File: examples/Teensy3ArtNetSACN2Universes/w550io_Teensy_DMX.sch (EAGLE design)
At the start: 33 parts, among them IC1 MAX481CPA, IC2 MAX481CPA

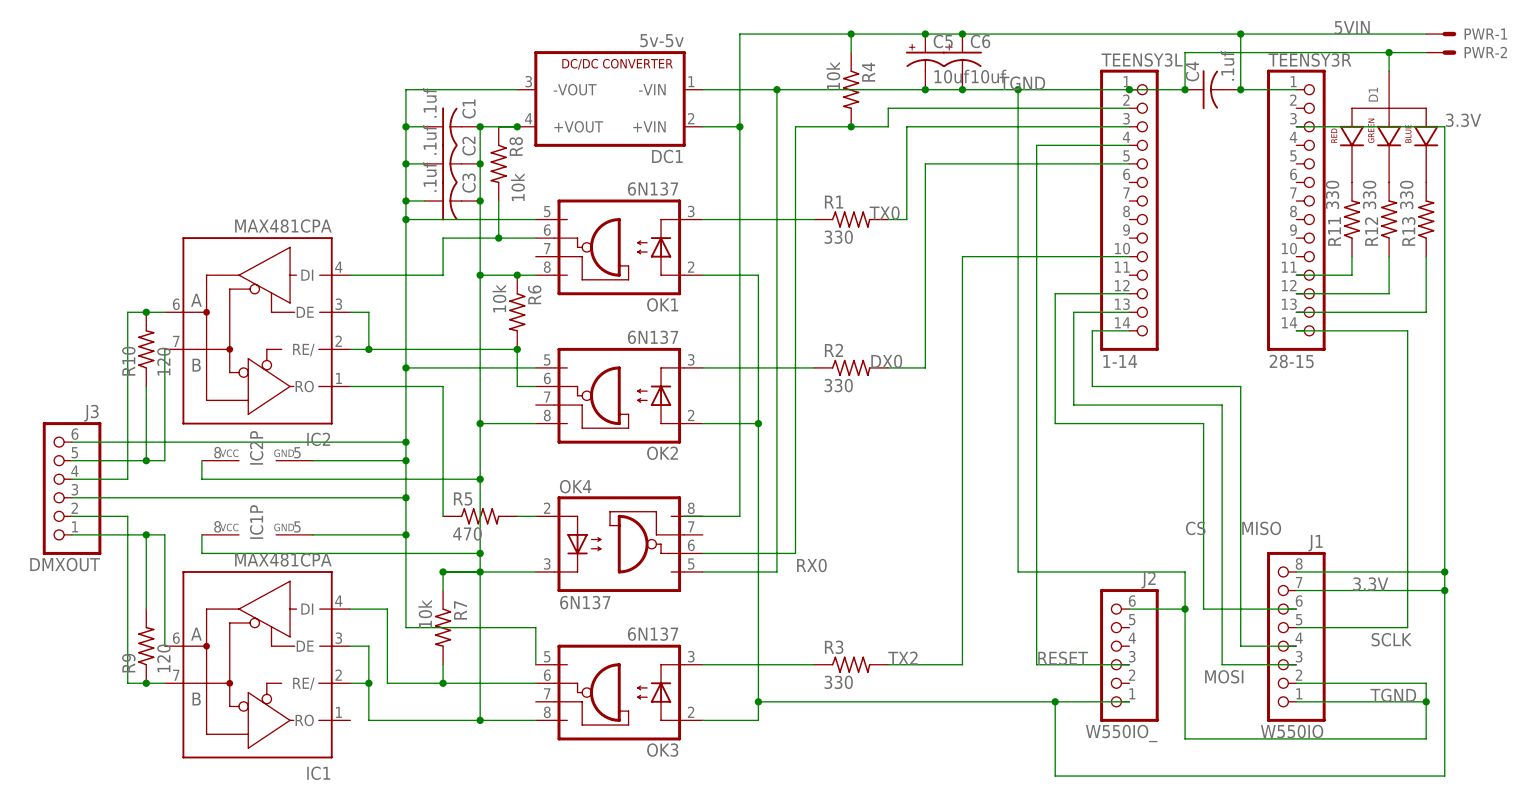
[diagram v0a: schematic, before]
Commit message: Change Board to output only
Bi-directional design power is unstable.  Previous design is functional
by not populating input and direction optocouplers.
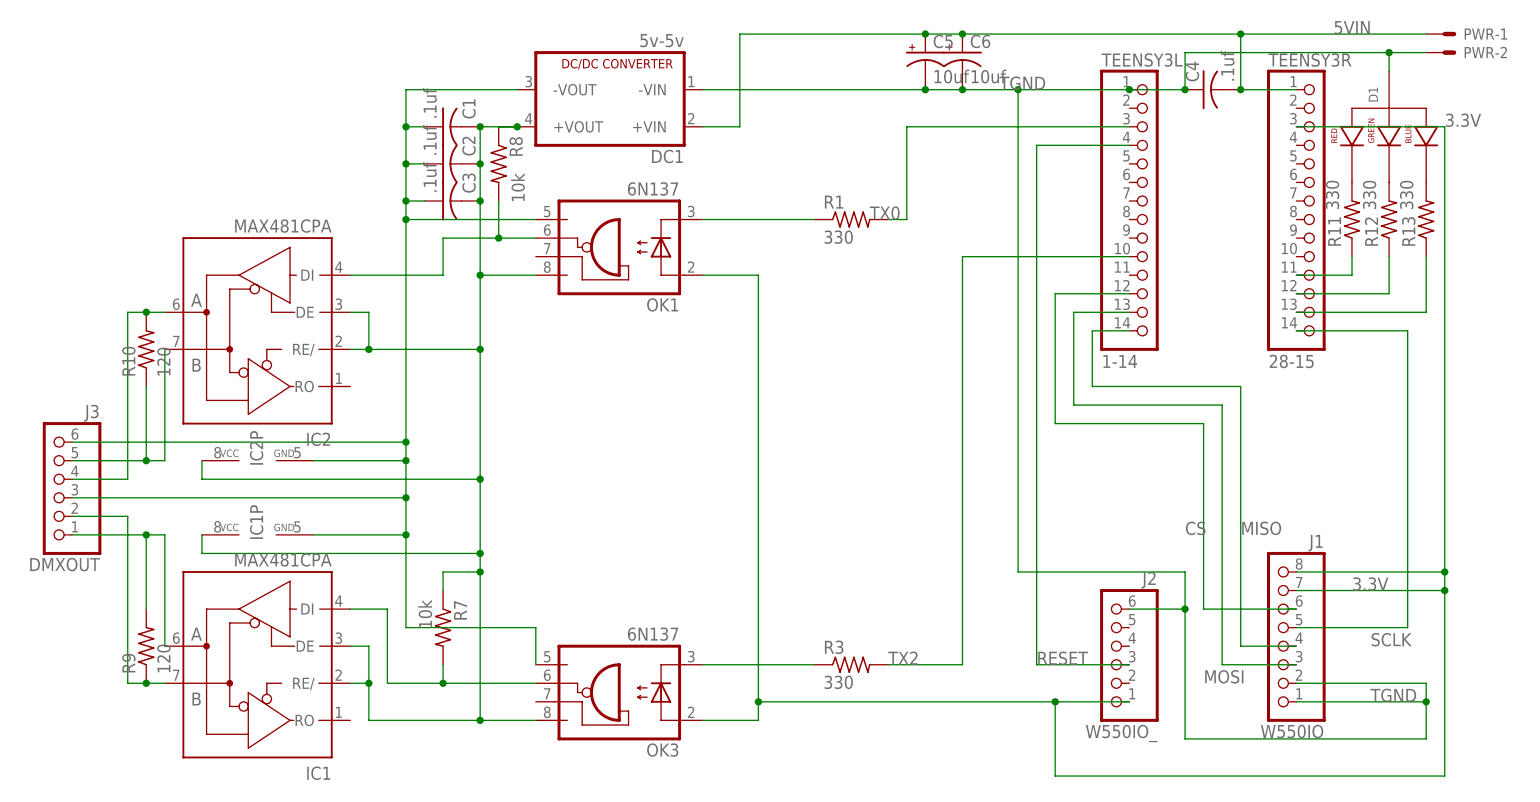
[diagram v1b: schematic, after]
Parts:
- removed OK2, OK4: 6N137, optocoupler:6N137
- removed R2: 330, adafruit:R-US_0204/5
- removed R4, R6: 10k, adafruit:R-US_0204/5
- removed R5: 470, adafruit:R-US_0204/5
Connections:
- removed net DX0: R2.2, TEENSY3L.5
- removed net N$1: OK4.A, R5.2
- removed net N$12: IC2G$1.RO, R5.1
- removed net N$13: IC2G$1.DE, IC2G$1.RE/, OK2.VO, R6.2
- removed net N$6: OK2.C, R2.1
- removed net RX0: OK4.VO, R4.2, TEENSY3L.2
- net 3.3V: no longer OK2.A
- net 5VIN: no longer R4.1
- net GND: no longer OK2.GND
- net TGND: no longer OK4.GND
- net VCC: now also IC2G$1.DE, IC2G$1.RE/; no longer OK2.VCC, OK4.C, R6.1

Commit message: Changed 10k Resistors to 1k
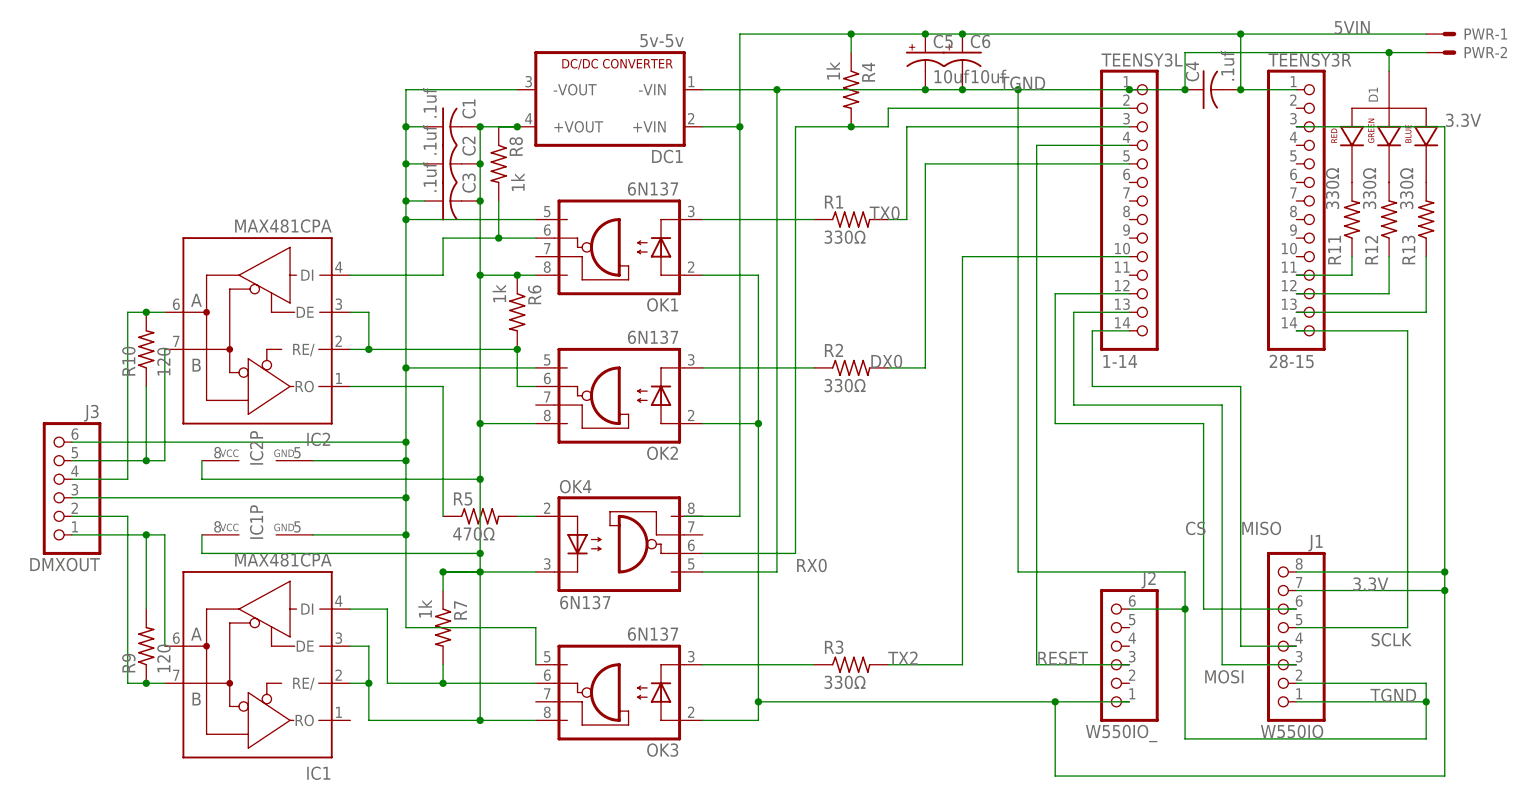
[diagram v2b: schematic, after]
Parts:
- added OK2, OK4: 6N137, optocoupler:6N137
- added R2: 330Ω, adafruit:R-US_0204/5
- added R4, R6: 1k, adafruit:R-US_0204/5
- added R5: 470Ω, adafruit:R-US_0204/5
- R1, R11, R12, R13, R3: value 330 -> 330Ω
- R7, R8: value 10k -> 1k
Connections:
- new net DX0: R2.2, TEENSY3L.5
- new net N$1: OK4.A, R5.2
- new net N$12: IC2G$1.RO, R5.1
- new net N$13: IC2G$1.DE, IC2G$1.RE/, OK2.VO, R6.2
- new net N$6: OK2.C, R2.1
- new net RX0: OK4.VO, R4.2, TEENSY3L.2
- net 3.3V: now also OK2.A
- net 5VIN: now also R4.1
- net GND: now also OK2.GND
- net TGND: now also OK4.GND
- net VCC: now also OK2.VCC, OK4.C, R6.1; no longer IC2G$1.DE, IC2G$1.RE/

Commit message: Changed resistors to 3.3k
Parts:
- R4: value 1k -> 10k
- R6, R7, R8: value 1k -> 3.3k
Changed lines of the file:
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@@
 <part name="R2" library="adafruit" deviceset="R-US_" device="0204/5" value="330Ω"/>
 <part name="R3" library="adafruit" deviceset="R-US_" device="0204/5" value="330Ω"/>
-<part name="R4" library="adafruit" deviceset="R-US_" device="0204/5" value="1k"/>
+<part name="R4" library="adafruit" deviceset="R-US_" device="0204/5" value="10k"/>
 <part name="IC1" library="maxim" deviceset="MAX481CPA" device=""/>
 <part name="IC2" library="maxim" deviceset="MAX481CPA" device=""/>
 <part name="DMXOUT" library="adafruit" deviceset="PINHD-1X6" device="B" value="J3"/>
 <part name="R5" library="adafruit" deviceset="R-US_" device="0204/5" value="470Ω"/>
-<part name="R6" library="adafruit" deviceset="R-US_" device="0204/5" value="1k"/>
-<part name="R7" library="adafruit" deviceset="R-US_" device="0204/5" value="1k"/>
-<part name="R8" library="adafruit" deviceset="R-US_" device="0204/5" value="1k"/>
+<part name="R6" library="adafruit" deviceset="R-US_" device="0204/5" value="3.3k"/>
+<part name="R7" library="adafruit" deviceset="R-US_" device="0204/5" value="3.3k"/>
+<part name="R8" library="adafruit" deviceset="R-US_" device="0204/5" value="3.3k"/>
 <part name="R9" library="adafruit" deviceset="R-US_" device="0204/5" value="120"/>
 <part name="R10" library="adafruit" deviceset="R-US_" device="0204/5" value="120"/>

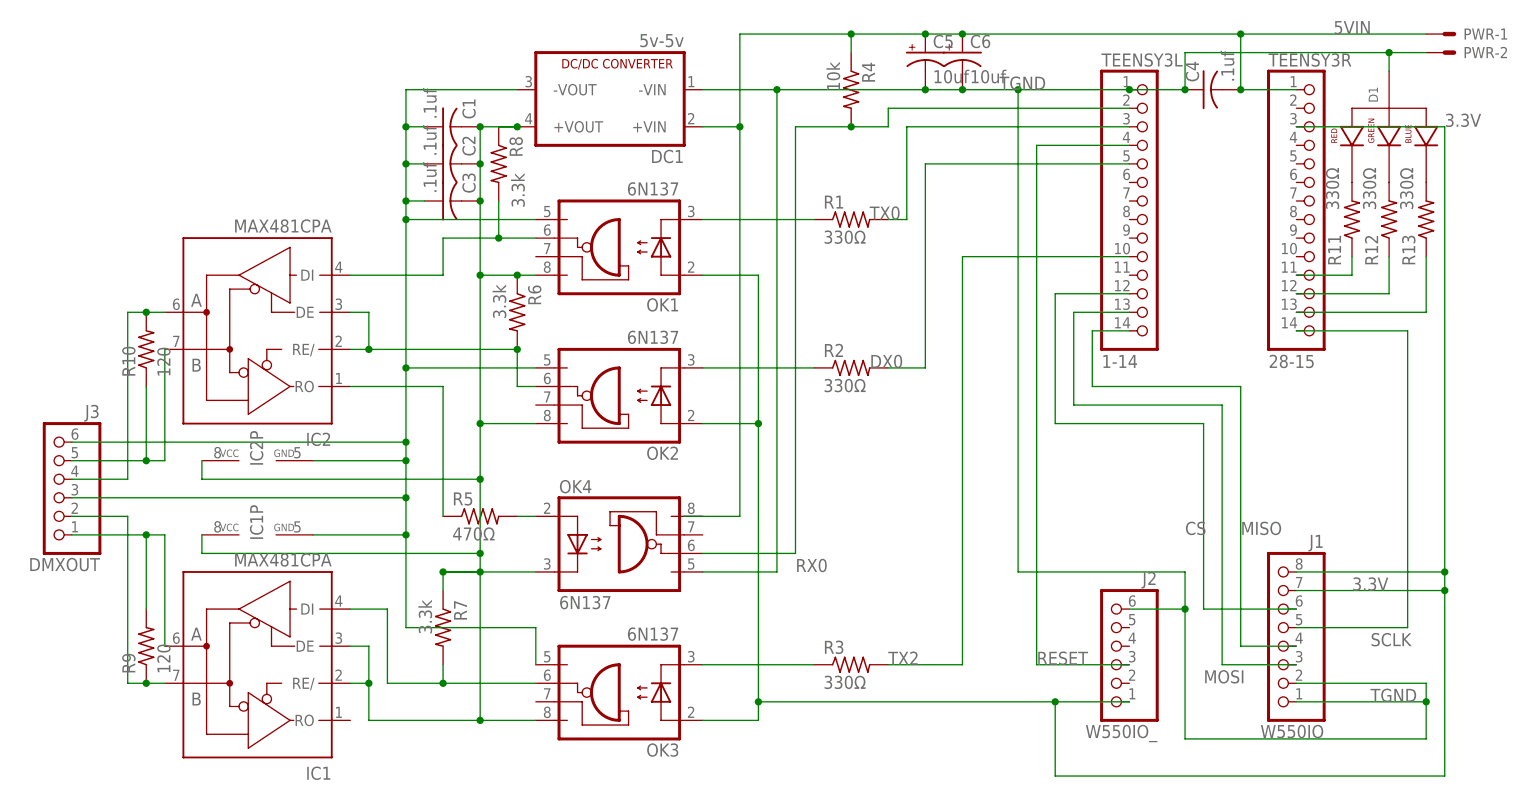
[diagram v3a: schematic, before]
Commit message: Fix DMX input / example schematic
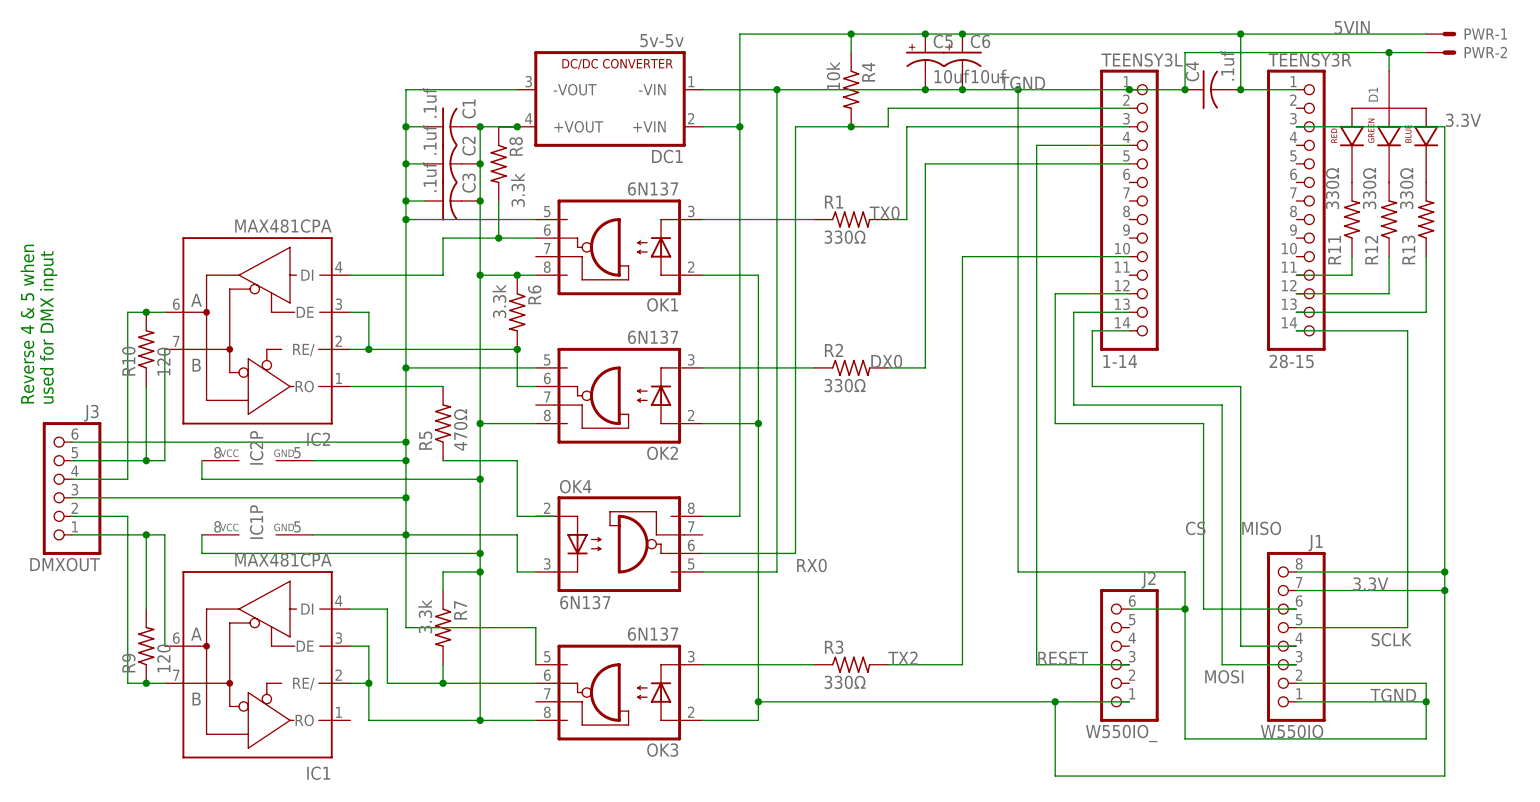
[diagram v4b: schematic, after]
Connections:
- net 5VIN: now also OK4.VCC
- net GND: now also OK4.C
- net N$1: now also R5.1; no longer R5.2
- net N$12: now also R5.2; no longer R5.1
- net VCC: no longer OK4.C
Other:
- note added: "Reverse 4 & 5 when used for DMX input"
- moved on the sheet: R5
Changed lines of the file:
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@@
 <sheet>
 <plain>
+<text x="-15.24" y="40.64" size="1.778" layer="91" rot="R90">Reverse 4 &amp; 5 when
+used for DMX input</text>
 </plain>
 <instances>
@@
 <attribute name="VALUE" x="-8.89" y="40.64" size="1.778" layer="96" rot="R180"/>
 </instance>
-<instance part="R5" gate="G$1" x="43.18" y="25.4"/>
+<instance part="R5" gate="G$1" x="38.1" y="38.1" rot="R90"/>
 <instance part="R6" gate="G$1" x="48.26" y="53.34" rot="R270"/>
 <instance part="R7" gate="G$1" x="38.1" y="10.16" rot="R270"/>
@@
 <junction x="147.32" y="91.44"/>
 <label x="160.02" y="91.44" size="1.778" layer="95"/>
-<wire x1="78.74" y1="78.74" x2="78.74" y2="25.4" width="0.1524" layer="91"/>
-<wire x1="78.74" y1="25.4" x2="71.12" y2="25.4" width="0.1524" layer="91"/>
-<junction x="78.74" y="78.74"/>
 <pinref part="C5" gate="G$1" pin="+"/>
 <junction x="104.14" y="91.44"/>
 <pinref part="C6" gate="G$1" pin="+"/>
 <junction x="109.22" y="91.44"/>
+<wire x1="78.74" y1="25.4" x2="78.74" y2="78.74" width="0.1524" layer="91"/>
+<junction x="78.74" y="78.74"/>
+<pinref part="OK4" gate="A" pin="VCC"/>
+<wire x1="78.74" y1="25.4" x2="73.66" y2="25.4" width="0.1524" layer="91"/>
 </segment>
 </net>
@@
 <wire x1="50.8" y1="5.08" x2="50.8" y2="10.16" width="0.1524" layer="91"/>
 <wire x1="50.8" y1="10.16" x2="33.02" y2="10.16" width="0.1524" layer="91"/>
+<wire x1="33.02" y1="22.86" x2="48.26" y2="22.86" width="0.1524" layer="91"/>
+<pinref part="OK4" gate="A" pin="C"/>
+<wire x1="50.8" y1="17.78" x2="48.26" y2="17.78" width="0.1524" layer="91"/>
+<wire x1="48.26" y1="22.86" x2="48.26" y2="17.78" width="0.1524" layer="91"/>
 </segment>
 </net>
@@
 <junction x="43.18" y="68.58"/>
 <junction x="43.18" y="58.42"/>
-<pinref part="OK4" gate="A" pin="C"/>
 <wire x1="43.18" y1="38.1" x2="43.18" y2="30.48" width="0.1524" layer="91"/>
 <wire x1="43.18" y1="30.48" x2="43.18" y2="20.32" width="0.1524" layer="91"/>
 <wire x1="43.18" y1="20.32" x2="43.18" y2="17.78" width="0.1524" layer="91"/>
 <wire x1="43.18" y1="17.78" x2="43.18" y2="-2.54" width="0.1524" layer="91"/>
-<wire x1="50.8" y1="17.78" x2="38.1" y2="17.78" width="0.1524" layer="91"/>
 <pinref part="OK3" gate="A" pin="VCC"/>
 <wire x1="38.1" y1="17.78" x2="43.18" y2="17.78" width="0.1524" layer="91"/>
@@
 <pinref part="R7" gate="G$1" pin="1"/>
 <wire x1="38.1" y1="15.24" x2="38.1" y2="17.78" width="0.1524" layer="91"/>
-<junction x="38.1" y="17.78"/>
 <pinref part="R8" gate="G$1" pin="1"/>
 <wire x1="45.72" y1="78.74" x2="48.26" y2="78.74" width="0.1524" layer="91"/>
@@
 </segment>
 </net>
-<net name="N$1" class="0">
-<segment>
-<pinref part="OK4" gate="A" pin="A"/>
-<pinref part="R5" gate="G$1" pin="2"/>
-<wire x1="48.26" y1="25.4" x2="50.8" y2="25.4" width="0.1524" layer="91"/>
-</segment>
-</net>
 <net name="N$12" class="0">
 <segment>
-<pinref part="R5" gate="G$1" pin="1"/>
-<wire x1="38.1" y1="25.4" x2="38.1" y2="43.18" width="0.1524" layer="91"/>
 <pinref part="IC2" gate="G$1" pin="RO"/>
 <wire x1="38.1" y1="43.18" x2="25.4" y2="43.18" width="0.1524" layer="91"/>
+<pinref part="R5" gate="G$1" pin="2"/>
 </segment>
 </net>
@@
 </segment>
 </net>
+<net name="N$1" class="0">
+<segment>
+<pinref part="R5" gate="G$1" pin="1"/>
+<wire x1="48.26" y1="33.02" x2="38.1" y2="33.02" width="0.1524" layer="91"/>
+<wire x1="48.26" y1="33.02" x2="48.26" y2="25.4" width="0.1524" layer="91"/>
+<pinref part="OK4" gate="A" pin="A"/>
+<wire x1="48.26" y1="25.4" x2="50.8" y2="25.4" width="0.1524" layer="91"/>
+<wire x1="50.8" y1="25.4" x2="53.34" y2="25.4" width="0.1524" layer="91"/>
+</segment>
+</net>
 </nets>
 </sheet>
@@
 </schematic>
 </drawing>
+<compatibility>
+<note version="6.3" minversion="6.2.2" severity="warning">
+Since Version 6.2.2 text objects can contain more than one line,
+which will not be processed correctly with this version.
+</note>
+</compatibility>
 </eagle>
